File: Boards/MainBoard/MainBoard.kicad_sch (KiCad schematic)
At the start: 28 parts, among them J1 Conn_02x08_Counter_Clockwise, J11 Conn_02x10_Counter_Clockwise, J12 Conn_02x10_Counter_Clockwise, J13 Conn_02x10_Counter_Clockwise, J14 Conn_02x10_Counter_Clockwise, J2 Conn_02x08_Counter_Clockwise, J3 Conn_02x08_Counter_Clockwise, J4 TBP01R1-508-06BE, J5 Conn_02x10_Counter_Clockwise, J6 TBP01R2-508-06BE

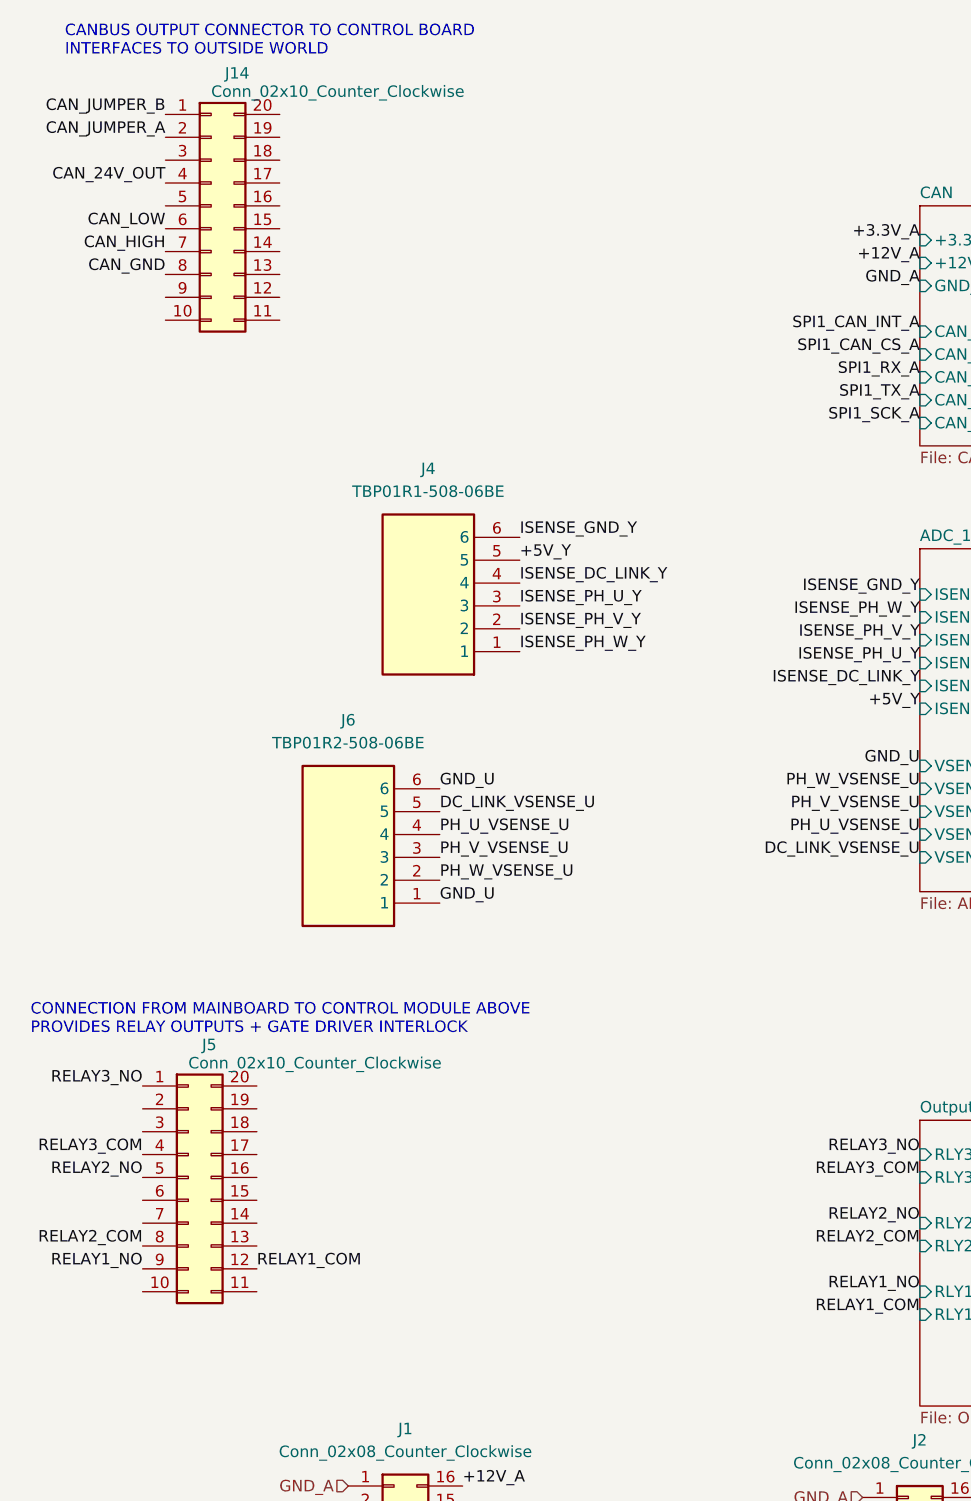
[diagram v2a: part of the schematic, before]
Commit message: fix connector pinout
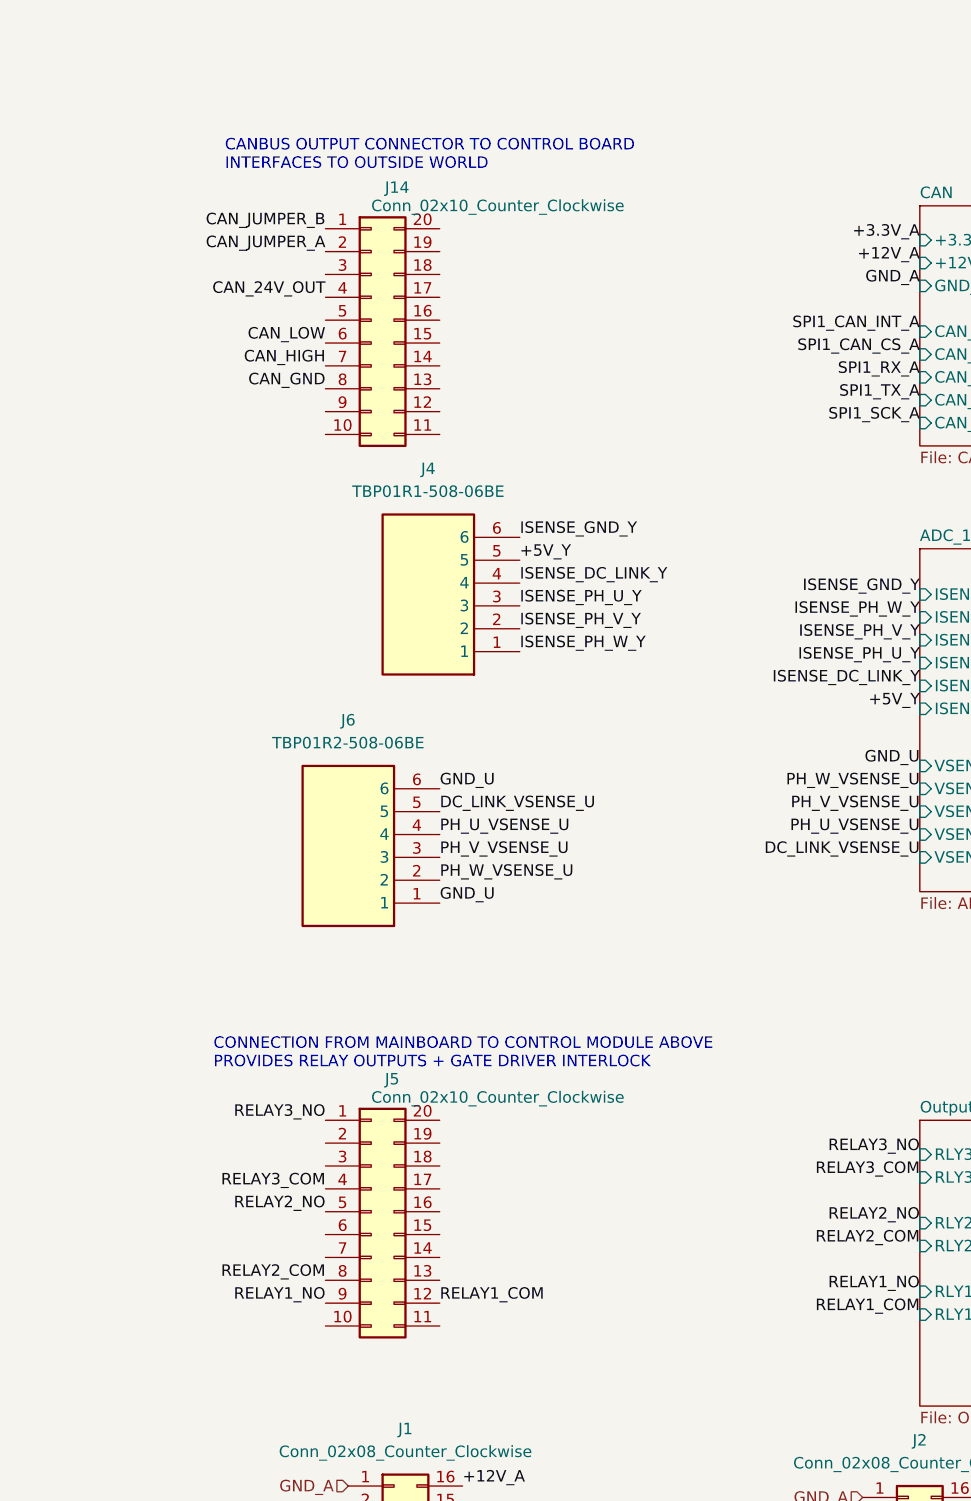
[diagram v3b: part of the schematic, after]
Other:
- moved on the sheet: J14, J5
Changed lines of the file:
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@@
 	(text "CANBUS OUTPUT CONNECTOR TO CONTROL BOARD\nINTERFACES TO OUTSIDE WORLD"
 		(exclude_from_sim no)
-		(at 6.604 7.112 0)
+		(at 24.384 19.812 0)
 		(effects
 			(font
@@
 	(text "CONNECTION FROM MAINBOARD TO CONTROL MODULE ABOVE\nPROVIDES RELAY OUTPUTS + GATE DRIVER INTERLOCK"
 		(exclude_from_sim no)
-		(at 2.794 115.824 0)
+		(at 23.114 119.634 0)
 		(effects
 			(font
@@
 	)
 	(label "CAN_24V_OUT"
-		(at 17.78 22.86 180)
+		(at 35.56 35.56 180)
 		(effects
 			(font
@@
 	)
 	(label "CAN_HIGH"
-		(at 17.78 30.48 180)
+		(at 35.56 43.18 180)
 		(effects
 			(font
@@
 	)
 	(label "CAN_JUMPER_A"
-		(at 17.78 17.78 180)
+		(at 35.56 30.48 180)
 		(effects
 			(font
@@
 	)
 	(label "RELAY2_COM"
-		(at 15.24 140.97 180)
+		(at 35.56 144.78 180)
 		(effects
 			(font
@@
 	)
 	(label "RELAY2_NO"
-		(at 15.24 133.35 180)
+		(at 35.56 137.16 180)
 		(effects
 			(font
@@
 	)
 	(label "RELAY1_NO"
-		(at 15.24 143.51 180)
+		(at 35.56 147.32 180)
 		(effects
 			(font
@@
 	)
 	(label "CAN_GND"
-		(at 17.78 33.02 180)
+		(at 35.56 45.72 180)
 		(effects
 			(font
@@
 	)
 	(label "CAN_JUMPER_B"
-		(at 17.78 15.24 180)
+		(at 35.56 27.94 180)
 		(effects
 			(font
@@
 	)
 	(label "RELAY3_NO"
-		(at 15.24 123.19 180)
+		(at 35.56 127 180)
 		(effects
 			(font
@@
 	)
 	(label "CAN_LOW"
-		(at 17.78 27.94 180)
+		(at 35.56 40.64 180)
 		(effects
 			(font
@@
 	)
 	(label "RELAY3_COM"
-		(at 15.24 130.81 180)
+		(at 35.56 134.62 180)
 		(effects
 			(font
@@
 	)
 	(label "RELAY1_COM"
-		(at 27.94 143.51 0)
+		(at 48.26 147.32 0)
 		(effects
 			(font
@@
 	(symbol
 		(lib_id "Connector_Generic:Conn_02x10_Counter_Clockwise")
-		(at 22.86 25.4 0)
+		(at 40.64 38.1 0)
 		(unit 1)
 		(exclude_from_sim no)
@@
 		(dnp no)
 		(property "Reference" "J14"
-			(at 24.384 10.668 0)
+			(at 42.164 23.368 0)
 			(effects
 				(font
@@
 		)
 		(property "Value" "Conn_02x10_Counter_Clockwise"
-			(at 22.8601 12.7 0)
+			(at 40.6401 25.4 0)
 			(effects
 				(font
@@
 		)
 		(property "Footprint" "Connector_PinHeader_2.54mm:PinHeader_2x10_P2.54mm_Vertical"
-			(at 22.86 25.4 0)
+			(at 40.64 38.1 0)
 			(effects
 				(font
@@
 		)
 		(property "Datasheet" "~"
-			(at 22.86 25.4 0)
+			(at 40.64 38.1 0)
 			(effects
 				(font
@@
 		)
 		(property "Description" "Generic connector, double row, 02x10, counter clockwise pin numbering scheme (similar to DIP package numbering), script generated (kicad-library-utils/schlib/autogen/connector/)"
-			(at 22.86 25.4 0)
+			(at 40.64 38.1 0)
 			(effects
 				(font
@@
 	(symbol
 		(lib_id "Connector_Generic:Conn_02x10_Counter_Clockwise")
-		(at 20.32 133.35 0)
+		(at 40.64 137.16 0)
 		(unit 1)
 		(exclude_from_sim no)
@@
 		(dnp no)
 		(property "Reference" "J5"
-			(at 21.844 118.618 0)
+			(at 42.164 122.428 0)
 			(effects
 				(font
@@
 		)
 		(property "Value" "Conn_02x10_Counter_Clockwise"
-			(at 20.3201 120.65 0)
+			(at 40.6401 124.46 0)
 			(effects
 				(font
@@
 		)
 		(property "Footprint" "Connector_PinHeader_2.54mm:PinHeader_2x10_P2.54mm_Vertical"
-			(at 20.32 133.35 0)
+			(at 40.64 137.16 0)
 			(effects
 				(font
@@
 		)
 		(property "Datasheet" "~"
-			(at 20.32 133.35 0)
+			(at 40.64 137.16 0)
 			(effects
 				(font
@@
 		)
 		(property "Description" "Generic connector, double row, 02x10, counter clockwise pin numbering scheme (similar to DIP package numbering), script generated (kicad-library-utils/schlib/autogen/connector/)"
-			(at 20.32 133.35 0)
-			(effects
-				(font
+			(at 40.64 137.16 0)
+			(effects
+				(font
